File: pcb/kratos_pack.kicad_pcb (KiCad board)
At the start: 4 copper layers, 44.2 x 20.2 mm, 121 parts, among them J1 USB_C_Receptacle_USB2.0, J2 PROG_CONN, J3 DBG_UART, J4 BAT_MID+NTC, J5 BAT_7.4V, J6 BAT_0V, J7 OUT+, J8 OUT-, Q1 AON7403, Q2 AON7414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

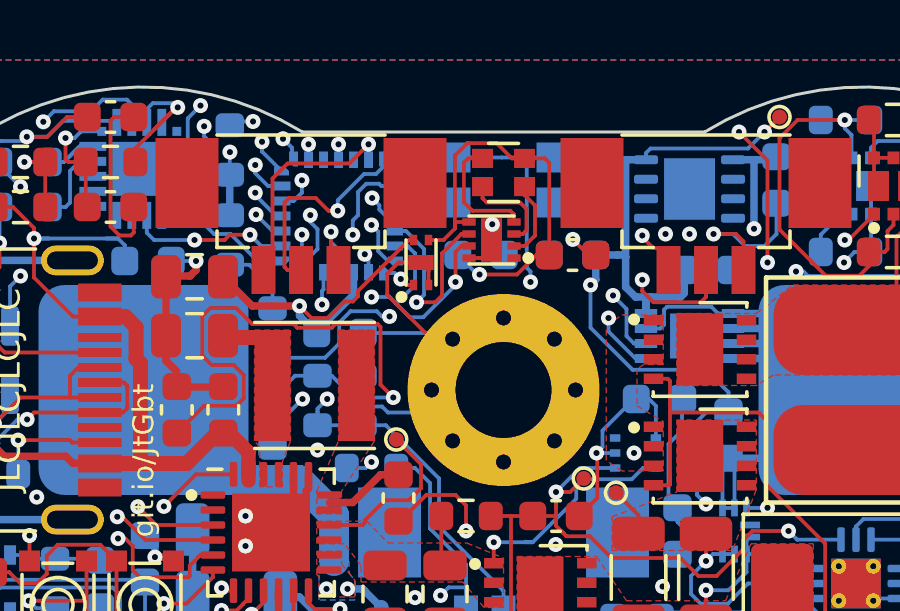
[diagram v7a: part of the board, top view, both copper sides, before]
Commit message: PCB: update silk screen
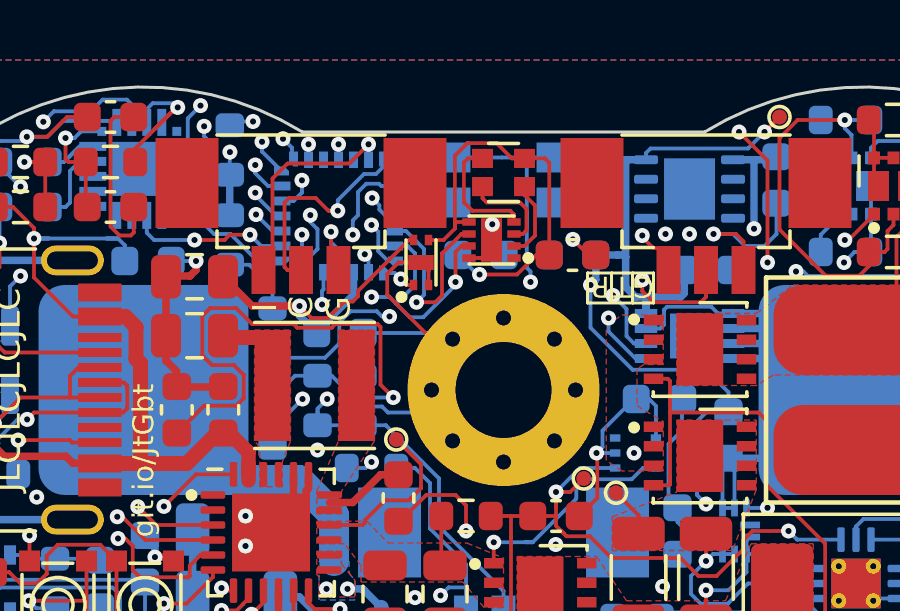
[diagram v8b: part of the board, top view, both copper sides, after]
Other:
- board text added: "C"
- board text added: "G"
- board text added: "I"
- board text added: "T"
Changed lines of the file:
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@@
     )
   )
+  (gr_line (start 149.25 107.4) (end 149.25 108.45) (layer "B.SilkS") (width 0.1))
   (gr_circle (center 162.25 104.25) (end 162.35 104.25) (layer "B.SilkS") (width 0.2) (fill none))
   (gr_circle (center 159.25 97.45) (end 159.35 97.45) (layer "B.SilkS") (width 0.2) (fill none))
+  (gr_line (start 147.4 107.4) (end 149.25 107.4) (layer "B.SilkS") (width 0.1))
   (gr_circle (center 161.95 91.75) (end 162.05 91.75) (layer "B.SilkS") (width 0.2) (fill none))
+  (gr_line (start 149.25 108.45) (end 147 108.45) (layer "B.SilkS") (width 0.1))
   (gr_circle (center 159.95 104.5) (end 160.05 104.5) (layer "B.SilkS") (width 0.2) (fill none))
+  (gr_line (start 147.75 107.4) (end 147.75 108.45) (layer "B.SilkS") (width 0.1))
   (gr_circle (center 137.05 93.85) (end 137.15 93.85) (layer "B.SilkS") (width 0.2) (fill none))
   (gr_circle (center 154.2 102.6) (end 154.3 102.6) (layer "B.SilkS") (width 0.2) (fill none))
   (gr_circle (center 133.25 104.85) (end 133.35 104.85) (layer "B.SilkS") (width 0.2) (fill none))
+  (gr_line (start 147 108.45) (end 147 107.75) (layer "B.SilkS") (width 0.1))
   (gr_circle (center 157.45 103.35) (end 157.55 103.35) (layer "B.SilkS") (width 0.2) (fill none))
   (gr_circle (center 167.65 93.95) (end 167.75 93.95) (layer "B.SilkS") (width 0.2) (fill none))
@@
   (gr_circle (center 134.55 101.2) (end 134.65 101.2) (layer "B.SilkS") (width 0.2) (fill none))
   (gr_circle (center 159.35 92.3) (end 159.45 92.3) (layer "B.SilkS") (width 0.2) (fill none))
+  (gr_line (start 148.5 107.4) (end 148.5 108.45) (layer "B.SilkS") (width 0.1))
   (gr_line (start 170.3 103.75) (end 170.3 96.25) (layer "F.SilkS") (width 0.15))
   (gr_line (start 170.3 103.75) (end 170.3 106.6) (layer "F.SilkS") (width 0.15))
   (gr_line (start 170.3 96.25) (end 159.75 96.25) (layer "F.SilkS") (width 0.15))
+  (gr_line (start 156 96.1) (end 156 97.1) (layer "F.SilkS") (width 0.1))
   (gr_circle (center 163.35 94.6) (end 163.45 94.6) (layer "F.SilkS") (width 0.2) (fill none))
+  (gr_line (start 154.6 96.1) (end 154.6 97.05) (layer "F.SilkS") (width 0.1))
   (gr_circle (center 140.6 103.5) (end 140.7 103.5) (layer "F.SilkS") (width 0.2) (fill none))
   (gr_circle (center 147.6 96.9) (end 147.7 96.9) (layer "F.SilkS") (width 0.2) (fill none))
   (gr_circle (center 150.05 105.8) (end 150.15 105.8) (layer "F.SilkS") (width 0.2) (fill none))
+  (gr_line (start 155.3 96.1) (end 155.3 97.1) (layer "F.SilkS") (width 0.1))
   (gr_line (start 159.75 103.75) (end 170.3 103.75) (layer "F.SilkS") (width 0.15))
   (gr_line (start 159.75 96.25) (end 159.75 103.75) (layer "F.SilkS") (width 0.15))
+  (gr_line (start 153.8 97.1) (end 153.8 96.1) (layer "F.SilkS") (width 0.1))
+  (gr_line (start 156 97.1) (end 153.8 97.1) (layer "F.SilkS") (width 0.1))
   (gr_circle (center 155.35 97.65) (end 155.45 97.65) (layer "F.SilkS") (width 0.2) (fill none))
   (gr_line (start 170.3 96.275) (end 170.3 93.525) (layer "F.SilkS") (width 0.15))
   (gr_circle (center 151.825 95.6) (end 151.925 95.6) (layer "F.SilkS") (width 0.2) (fill none))
+  (gr_line (start 153.8 96.1) (end 156 96.1) (layer "F.SilkS") (width 0.1))
   (gr_circle (center 155.35 101.25) (end 155.45 101.25) (layer "F.SilkS") (width 0.2) (fill none))
   (gr_line (start 157.703774 91.400001) (end 144.296226 91.400001) (layer "Edge.Cuts") (width 0.1))
@@
   (gr_line (start 144.296226 108.6) (end 157.703774 108.6) (layer "Edge.Cuts") (width 0.1))
   (gr_arc (start 139 100) (end 144.296226 91.400001) (angle -243.2528568) (layer "Edge.Cuts") (width 0.1))
+  (gr_text "B" (at 147.4 108) (layer "B.SilkS")
+    (effects (font (size 0.7 0.7) (thickness 0.12)) (justify mirror))
+  )
+  (gr_text "G" (at 148.85 108) (layer "B.SilkS")
+    (effects (font (size 0.7 0.7) (thickness 0.12)) (justify mirror))
+  )
+  (gr_text "T" (at 148.15 108) (layer "B.SilkS")
+    (effects (font (size 0.7 0.7) (thickness 0.12)) (justify mirror))
+  )
+  (gr_text "C" (at 144.25 97.25 90) (layer "F.SilkS")
+    (effects (font (size 0.8 0.8) (thickness 0.15)))
+  )
   (gr_text "-\n" (at 166.8 102.2 90) (layer "F.SilkS")
     (effects (font (size 1.5 1.5) (thickness 0.3)))
@@
   (gr_text "TheColonelYoung\nGitHub" (at 171.6 100 90) (layer "F.SilkS")
     (effects (font (size 0.8 0.8) (thickness 0.15)))
+  )
+  (gr_text "R" (at 154.2 96.55 180) (layer "F.SilkS")
+    (effects (font (size 0.7 0.7) (thickness 0.12)))
   )
   (gr_text "5.8-8.4V\nmax. 5A" (at 169 100 90) (layer "F.SilkS")
@@
     (effects (font (size 0.7 0.7) (thickness 0.15)))
   )
+  (gr_text "G" (at 155.65 96.55 180) (layer "F.SilkS")
+    (effects (font (size 0.7 0.7) (thickness 0.12)))
+  )
   (gr_text "R" (at 139.1 109 90) (layer "F.SilkS")
     (effects (font (size 0.7 0.7) (thickness 0.15)))
+  )
+  (gr_text "I" (at 143.05 97.25 90) (layer "F.SilkS")
+    (effects (font (size 0.8 0.8) (thickness 0.15)))
   )
   (gr_text "B" (at 136.2 109.025 90) (layer "F.SilkS")
@@
     (effects (font (size 0.8 0.8) (thickness 0.15)))
   )
+  (gr_text "G" (at 145.5 97.3 90) (layer "F.SilkS")
+    (effects (font (size 0.8 0.8) (thickness 0.15)))
+  )
+  (gr_text "T" (at 154.95 96.55 180) (layer "F.SilkS")
+    (effects (font (size 0.7 0.7) (thickness 0.12)))
+  )
   (gr_text "JLCJLCJLCJLC" (at 134.5 100 90) (layer "F.SilkS")
